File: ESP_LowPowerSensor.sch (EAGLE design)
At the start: 2 parts

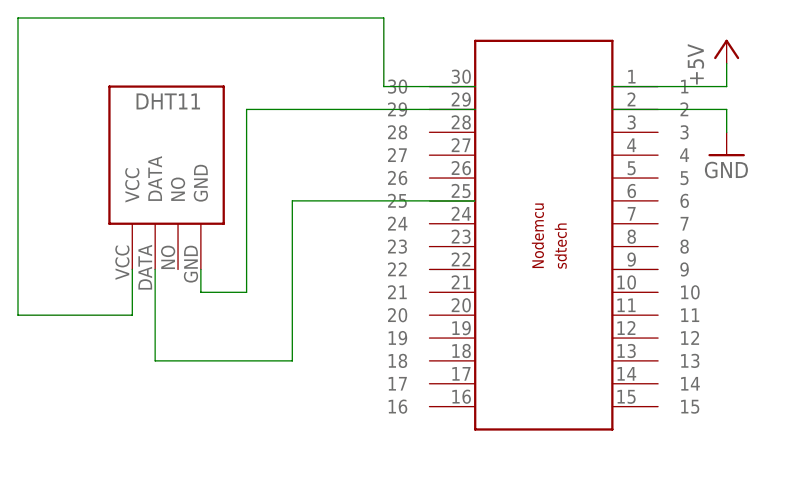
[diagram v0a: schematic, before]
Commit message: feat: add a connection between pin D0 and RST
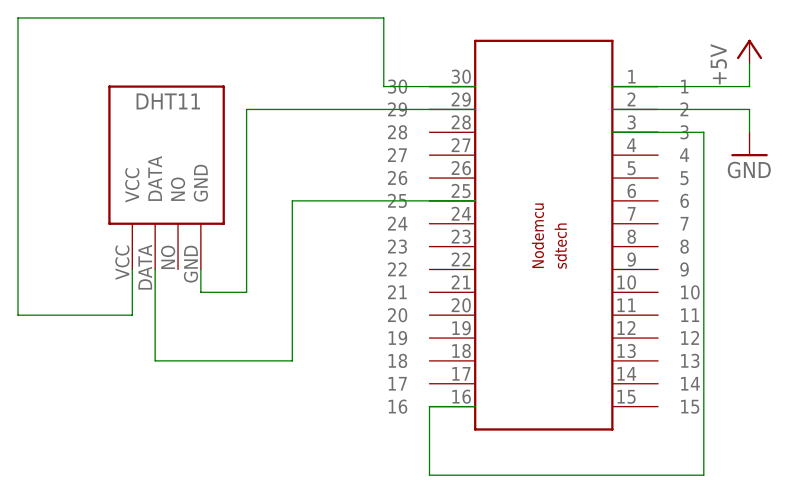
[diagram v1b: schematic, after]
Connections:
- new net N$1: U$1.16, U$1.3
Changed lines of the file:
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@@
 <instances>
 <instance part="U$1" gate="G$1" x="86.36" y="55.88" smashed="yes"/>
-<instance part="GND1" gate="1" x="88.9" y="66.04" smashed="yes">
-<attribute name="VALUE" x="86.36" y="63.5" size="1.778" layer="96"/>
+<instance part="GND1" gate="1" x="91.44" y="66.04" smashed="yes">
+<attribute name="VALUE" x="88.9" y="63.5" size="1.778" layer="96"/>
 </instance>
-<instance part="P+1" gate="1" x="88.9" y="78.74" smashed="yes">
-<attribute name="VALUE" x="86.36" y="73.66" size="1.778" layer="96" rot="R90"/>
+<instance part="P+1" gate="1" x="91.44" y="78.74" smashed="yes">
+<attribute name="VALUE" x="88.9" y="73.66" size="1.778" layer="96" rot="R90"/>
 </instance>
 <instance part="U$2" gate="G$1" x="25.4" y="66.04" smashed="yes"/>
@@
 <segment>
 <pinref part="U$1" gate="G$1" pin="1"/>
-<wire x1="76.2" y1="73.66" x2="88.9" y2="73.66" width="0.1524" layer="91"/>
+<wire x1="76.2" y1="73.66" x2="91.44" y2="73.66" width="0.1524" layer="91"/>
 <pinref part="P+1" gate="1" pin="+5V"/>
-<wire x1="88.9" y1="73.66" x2="88.9" y2="76.2" width="0.1524" layer="91"/>
+<wire x1="91.44" y1="73.66" x2="91.44" y2="76.2" width="0.1524" layer="91"/>
 </segment>
 </net>
@@
 <segment>
 <pinref part="U$1" gate="G$1" pin="2"/>
-<wire x1="76.2" y1="71.12" x2="88.9" y2="71.12" width="0.1524" layer="91"/>
+<wire x1="76.2" y1="71.12" x2="91.44" y2="71.12" width="0.1524" layer="91"/>
 <pinref part="GND1" gate="1" pin="GND"/>
-<wire x1="88.9" y1="71.12" x2="88.9" y2="68.58" width="0.1524" layer="91"/>
+<wire x1="91.44" y1="71.12" x2="91.44" y2="68.58" width="0.1524" layer="91"/>
 </segment>
 </net>
@@
 </segment>
 </net>
+<net name="N$1" class="0">
+<segment>
+<pinref part="U$1" gate="G$1" pin="16"/>
+<wire x1="60.96" y1="38.1" x2="55.88" y2="38.1" width="0.1524" layer="91"/>
+<wire x1="55.88" y1="38.1" x2="55.88" y2="30.48" width="0.1524" layer="91"/>
+<wire x1="55.88" y1="30.48" x2="86.36" y2="30.48" width="0.1524" layer="91"/>
+<wire x1="86.36" y1="30.48" x2="86.36" y2="68.58" width="0.1524" layer="91"/>
+<pinref part="U$1" gate="G$1" pin="3"/>
+<wire x1="86.36" y1="68.58" x2="76.2" y2="68.58" width="0.1524" layer="91"/>
+</segment>
+</net>
